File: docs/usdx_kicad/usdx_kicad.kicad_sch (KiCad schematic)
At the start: 0 parts

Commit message: Add KiCad PCB build files and ignore local artifacts
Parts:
- added C1, C29, C4: 1000u, Capacitor_THT:CP_Radial_D10.0mm_P5.00mm, symbol Device:C_Polarized
- added C10, C2, C3: 1n, Capacitor_THT:C_Disc_D5.0mm_W2.5mm_P5.00mm, symbol Device:C
- added C11, C12: 100p, Capacitor_THT:C_Disc_D5.0mm_W2.5mm_P5.00mm, symbol Device:C
- added C13, C18, C19, C21, C23, C26, C27: 100n, Capacitor_THT:C_Disc_D5.0mm_W2.5mm_P5.00mm, symbol Device:C
- added C14: 1u, Capacitor_THT:C_Disc_D5.0mm_W2.5mm_P5.00mm, symbol Device:C
- added C15, C16, C17, C20, C22, C24, C25, C28: 10u, Capacitor_THT:C_Disc_D5.0mm_W2.5mm_P5.00mm, symbol Device:C
- added C5, C6, C7, C8: 1n, Capacitor_THT:C_Rect_L11.5mm_W5.0mm_P10.00mm_MKT, symbol Device:C
- added C9: 470n, Capacitor_THT:C_Disc_D5.0mm_W2.5mm_P5.00mm, symbol Device:C
- added FST1: (no value), myFootprintLibrary:FST3253_board, symbol mySymbolLibrary:FST3253_board
- added J1: RX input, Connector_Coaxial:SMA_Molex_73251-1153_EdgeMount_Horizontal, symbol Connector:Conn_Coaxial
- added J10: Speaker, Connector_PinHeader_2.54mm:PinHeader_1x02_P2.54mm_Vertical, symbol Connector:Conn_01x02_Pin
- added J11: Power Connector, Connector_JST:JST_XH_B2B-XH-A_1x02_P2.50mm_Vertical, symbol Connector:Conn_01x02_Pin
- added J12: +12V, Connector_JST:JST_XH_B2B-XH-A_1x02_P2.50mm_Vertical, symbol Connector:Conn_01x02_Pin
- added J13: MCP23017, Connector_PinHeader_2.54mm:PinHeader_1x04_P2.54mm_Vertical, symbol Connector:Conn_01x04_Pin
- added J2: CLK2 output, Connector_Coaxial:SMA_Molex_73251-1153_EdgeMount_Horizontal, symbol Connector:Conn_Coaxial
- added J3: SSD1309, Connector_PinHeader_2.54mm:PinHeader_1x04_P2.54mm_Vertical, symbol Connector:Conn_01x04_Pin
- added J4: PWR SWR meter, Connector_PinHeader_2.54mm:PinHeader_1x03_P2.54mm_Vertical, symbol Connector:Conn_01x03_Pin
- added J5: W5500, Connector_PinHeader_2.54mm:PinHeader_1x08_P2.54mm_Vertical, symbol Connector:Conn_01x08_Pin
- added J6: ROT_MENU, Connector_PinHeader_2.54mm:PinHeader_1x05_P2.54mm_Vertical, symbol Connector:Conn_01x05_Pin
- added J7: ROT_FREQ, Connector_PinHeader_2.54mm:PinHeader_1x05_P2.54mm_Vertical, symbol Connector:Conn_01x05_Pin
- added J8: Button Right, Connector_PinHeader_2.54mm:PinHeader_1x02_P2.54mm_Vertical, symbol Connector:Conn_01x02_Pin
- added J9: Button Left, Connector_PinHeader_2.54mm:PinHeader_1x02_P2.54mm_Vertical, symbol Connector:Conn_01x02_Pin
- added L1, L2, L3, L4, L5, L6: 1mH, myFootprintLibrary:choke, symbol Device:L_Ferrite_Small
- added LM2596_board1, LM2596_board2: (no value), myFootprintLibrary:LM2596_board, symbol mySymbolLibrary:LM2596_board
- added MAX98357_board1: (no value), myFootprintLibrary:MAX98357_board, symbol mySymbolLibrary:MAX98357_board
- added PCM1: (no value), myFootprintLibrary:PCM1808_board, symbol mySymbolLibrary:PCM1808_board
- added R1, R2: 82K, Resistor_THT:R_Axial_DIN0207_L6.3mm_D2.5mm_P7.62mm_Horizontal, symbol Device:R_US
- added R10, R11, R3, R4, R5, R6: 100, Resistor_THT:R_Axial_DIN0207_L6.3mm_D2.5mm_P7.62mm_Horizontal, symbol Device:R_US
- added R12, R9: 1K, Resistor_THT:R_Axial_DIN0207_L6.3mm_D2.5mm_P7.62mm_Horizontal, symbol Device:R_US
- added R7, R8: 10K, Resistor_THT:R_Axial_DIN0207_L6.3mm_D2.5mm_P7.62mm_Horizontal, symbol Device:R_US
- added SI5351_board1: SI5351_board, myFootprintLibrary:SI5351_board, symbol mySymbolLibrary:SI5351_board
- added T1: Transformer_1P_1S, myFootprintLibrary:transformer, symbol Device:Transformer_1P_1S
- added U1: ESP32-S3-DevKitC, Espressif:ESP32-S3-DevKitC, symbol Espressif:ESP32-S3-DevKitC
- added U2: LM4562, Package_DIP:DIP-8_W7.62mm, symbol Amplifier_Operational:LM4562
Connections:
- new net: C2.2, R2.2, R4.1, U2.2 (-)
- new net: C7.1, FST1.11 (2B2), R4.2
- new net: R6.1, U2.5 (+)
- new net: C6.1, FST1.10 (2B1), R6.2
- new net: C8.1, FST1.12 (2B3), R5.2
- new net: C5.1, FST1.13 (2B4), R3.2
- new net: FST1.14 (S0), SI5351_board1.6 (CLK1)
- new net: C21.1, C22.1, FST1.16 (VCC), L3.1
- new net: FST1.2 (S1), SI5351_board1.7 (CLK0)
- new net: FST1.9 (2A), T1.3 (SA)
- new net: C10.1, C16.1, C9.1, R7.1, R8.2, T1.4 (SB)
- new net: J10.1 (Pin_1), MAX98357_board1.8 (O+)
- new net: J10.2 (Pin_2), MAX98357_board1.9 (O-)
- new net: C25.1, C26.1, C4.1, J12.1 (Pin_1), L5.2, LM2596_board2.3 (IN+)
- new net: C2.1, PCM1.15 (RIN), R2.1, U2.1
- new net: L6.1, LM2596_board2.2 (OUT+)
- new net: C19.1, C20.1, L2.1, U2.8 (V+)
- new net: C3.1, PCM1.13 (LIN), R1.1, U2.7
- new net: C3.2, R1.2, R3.1, U2.6 (-)
- new net: C1.1, J11.1 (Pin_1), LM2596_board1.3 (IN+)
- new net: C17.1, C18.1, L1.1, PCM1.6 (VCC+5)
- new net: R10.1, U1.38 (GPIO41/MTDI)
- new net: C23.1, C24.1, L4.1, SI5351_board1.1 (VCC)
- new net: R11.1, U1.39 (GPIO42/MTMS)
- new net: J2.1 (In), SI5351_board1.5 (CLK2)
- new net: J1.1 (In), T1.1 (AA)
- new net: J1.2 (Ext), T1.2 (AB)
- new net: L5.1, LM2596_board1.2 (OUT+)
- new net: J4.1 (Pin_1), U1.5 (GPIO5/ADC1_CH4)
- new net: J4.2 (Pin_2), U1.4 (GPIO4/ADC1_CH3)
- new net: R5.1, U2.3 (+)
- new net: MAX98357_board1.5 (DIN), U1.10 (GPIO17/ADC2_CH6)
- new net: MAX98357_board1.6 (BCLK), U1.9 (GPIO16/ADC2_CH5/32K_N)
- new net: MAX98357_board1.7 (LRC), U1.8 (GPIO15/ADC2_CH4/32K_P)
- new net: J5.3 (Pin_3), U1.11 (GPIO18/ADC2_CH7)
- new net: J5.4 (Pin_4), U1.12 (GPIO8/ADC1_CH7)
- new net: J5.7 (Pin_7), U1.40 (GPIO2/ADC1_CH1)
- new net: J5.8 (Pin_8), U1.41 (GPIO1/ADC1_CH0)
- new net: J5.6 (Pin_6), U1.6 (GPIO6/ADC1_CH5)
- new net: J5.5 (Pin_5), U1.7 (GPIO7/ADC1_CH6)
- new net +3.3V: C13.1, C14.1, C15.1, J13.4 (Pin_4), J3.4 (Pin_4), J5.1 (Pin_1), J6.2 (Pin_2), J7.2 (Pin_2), PCM1.5 (VDD+3.3), PCM1.7 (VDD+3.3), R12.2, R9.2, U1.1 (3V3), U1.2 (3V3)
- new net +5V: C27.1, C28.1, C29.1, L1.2, L2.2, L3.2, L4.2, L6.2, MAX98357_board1.1 (VCC), R7.2, U1.21 (5V)
- new net BTN_L: J9.1 (Pin_1), U1.20 (GPIO14/ADC2_CH3)
- new net BTN_R: J8.1 (Pin_1), U1.19 (GPIO13/ADC2_CH2)
- new net GND: C1.2, C10.2, C11.2, C12.2, C13.2, C14.2, C15.2, C16.2, C17.2, C18.2, C19.2, C20.2, C21.2, C22.2, C23.2, C24.2, C25.2, C26.2, C27.2, C28.2, C29.2, C4.2, C5.2, C6.2, C7.2, C8.2, C9.2, FST1.1 (OE1), FST1.15 (OE2), FST1.8 (GND), J11.2 (Pin_2), J12.2 (Pin_2), J13.3 (Pin_3), J2.2 (Ext), J3.3 (Pin_3), J4.3 (Pin_3), J5.2 (Pin_2), J6.1 (Pin_1), J7.1 (Pin_1), J8.2 (Pin_2), J9.2 (Pin_2), LM2596_board1.1 (OUT-), LM2596_board1.4 (IN-), LM2596_board2.1 (OUT-), LM2596_board2.4 (IN-), MAX98357_board1.2 (GND), PCM1.14 (GND), PCM1.4 (GND), PCM1.8 (GND), R8.1, SI5351_board1.2 (GND), U1.22 (GND), U1.23 (GND), U1.24 (GND), U1.44 (GND), U2.4 (V-)
- new net I2C_SCL: C11.1, J13.2 (Pin_2), J3.2 (Pin_2), R11.2, R12.1, SI5351_board1.4 (SCL)
- new net I2C_SDA: C12.1, J13.1 (Pin_1), J3.1 (Pin_1), R10.2, R9.1, SI5351_board1.3 (SDA)
- new net I2S_BCK_PCM1808: PCM1.12 (BCK), U1.18 (GPIO12/ADC2_CH1)
- new net I2S_LRC_PCM1808: PCM1.10 (LRC), U1.16 (GPIO10/ADC1_CH9)
- new net I2S_OUT_PCM1808: PCM1.11 (OUT), U1.17 (GPIO11/ADC2_CH0)
- new net I2S_SCK_PCM1808: PCM1.9 (SCK), U1.15 (GPIO9/ADC1_CH8)
- new net ROT_FREQ_CLK: J7.5 (Pin_5), U1.27 (GPIO21)
- new net ROT_FREQ_DT: J7.4 (Pin_4), U1.28 (GPIO47)
- new net ROT_FREQ_SW: J7.3 (Pin_3), U1.30 (GPIO45)
- new net ROT_MENU_CLK: J6.5 (Pin_5), U1.35 (GPIO38)
- new net ROT_MENU_DT: J6.4 (Pin_4), U1.36 (GPIO39/MTCK)
- new net ROT_MENU_SW: J6.3 (Pin_3), U1.37 (GPIO40/MTDO)
- no-connect marks 0 -> 22
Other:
- company: (none) -> Guido Giorgetti - IW5ALZ

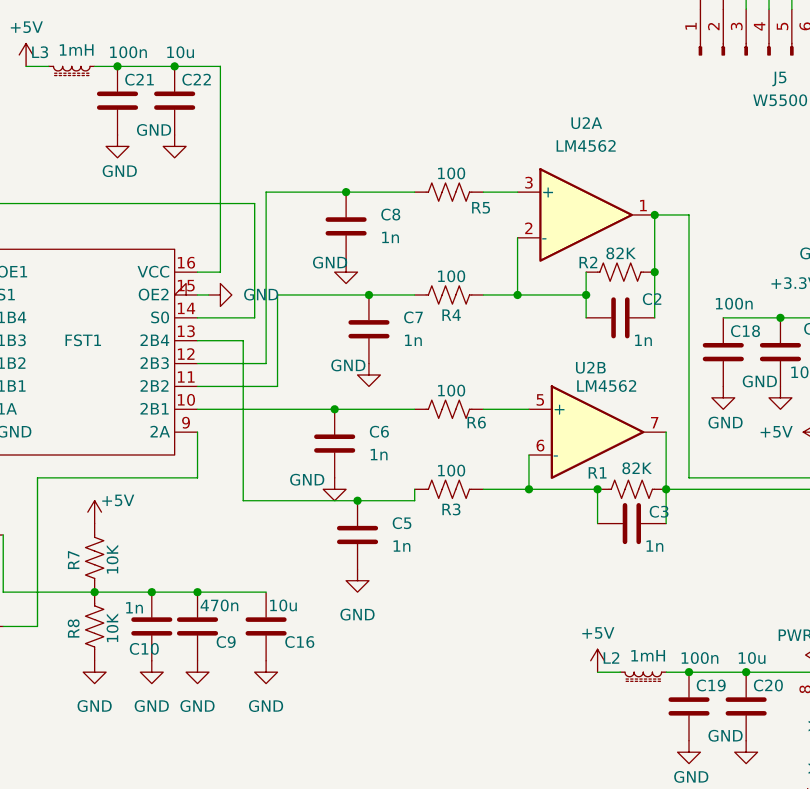
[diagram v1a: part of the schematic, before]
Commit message: LM4562 DC decoupling
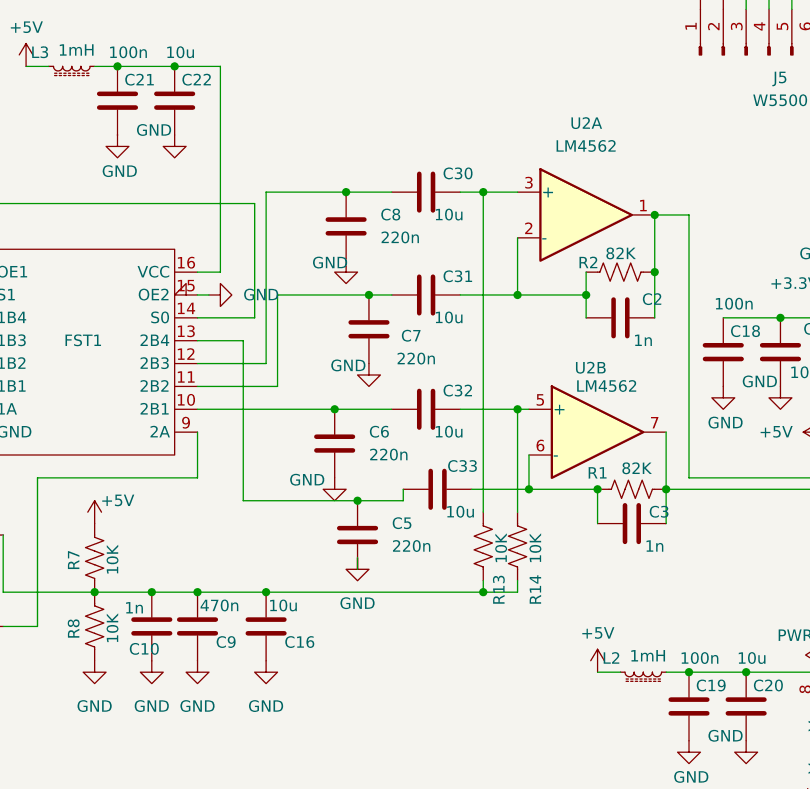
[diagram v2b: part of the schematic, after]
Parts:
- removed R3, R4, R5, R6: 100, Resistor_THT:R_Axial_DIN0207_L6.3mm_D2.5mm_P7.62mm_Horizontal, symbol Device:R_US
- added C30, C31, C32, C33: 10u, Capacitor_THT:C_Disc_D5.0mm_W2.5mm_P5.00mm, symbol Device:C
- added R13, R14: 10K, Resistor_THT:R_Axial_DIN0207_L6.3mm_D2.5mm_P7.62mm_Horizontal, symbol Device:R_US
- C5, C6, C7, C8: value 1n -> 220n
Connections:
- net at C2.2, R2.2, U2.2 (-): now also C31.1
- net at C7.1, FST1.11 (2B2): now also C31.2
- net at U2.5 (+): now also C32.1, R14.2
- net at C6.1, FST1.10 (2B1): now also C32.2
- net at C8.1, FST1.12 (2B3): now also C30.2
- net at C5.1, FST1.13 (2B4): now also C33.2
- net at C10.1, C16.1, C9.1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: now also R13.1, R14.1
- net at C3.2, R1.2, U2.6 (-): now also C33.1
- net at U2.3 (+): now also C30.1, R13.2

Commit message: PCB version 1.1
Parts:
- removed J1: RX input, Connector_Coaxial:SMA_Molex_73251-1153_EdgeMount_Horizontal, symbol Connector:Conn_Coaxial
- removed J2: CLK2 output, Connector_Coaxial:SMA_Molex_73251-1153_EdgeMount_Horizontal, symbol Connector:Conn_Coaxial
- added U3: RX Input, myFootprintLibrary:SMA connector, symbol mySymbolLibrary:SMA_Connector
- added U4: TX Out, myFootprintLibrary:SMA connector, symbol mySymbolLibrary:SMA_Connector
- U1: footprint Espressif:ESP32-S3-DevKitC -> myFootprintLibrary:ESP32-S3-DevKitC-Mine
- renumbered FST1 to FST3253
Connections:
- net GND: now also U4.1 (GND)
- net at SI5351_board1.5 (CLK2): now also U4.2 (RF)
- net at T1.1 (AA): now also U3.2 (RF)
- net at T1.2 (AB): now also U3.1 (GND)
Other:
- title: (none) -> FT8 ESP32

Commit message: capacitors voltage
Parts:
- C1: value 1000u -> 1000u 35V
- C29, C4: value 1000u -> 1000u 16V
- J11: value Power Connector -> Power Connector 19V
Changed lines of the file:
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@@
 		(dnp no)
 		(property "Reference" "C25"
-			(at 257.048 115.57 0)
+			(at 256.54 113.792 0)
 			(show_name no)
 			(do_not_autoplace no)
@@
 		)
 		(property "Value" "10u"
-			(at 259.334 124.46 0)
+			(at 256.794 116.586 0)
 			(show_name no)
 			(do_not_autoplace no)
@@
 			)
 		)
-		(property "Value" "Power Connector"
+		(property "Value" "Power Connector 19V"
 			(at 221.615 74.93 0)
 			(show_name no)
@@
 		(dnp no)
 		(property "Reference" "C26"
-			(at 252.222 119.634 0)
+			(at 250.698 113.792 0)
 			(show_name no)
 			(do_not_autoplace no)
@@
 			)
 		)
-		(property "Value" "1000u"
+		(property "Value" "1000u 35V"
 			(at 257.81 81.6609 0)
 			(show_name no)
@@
 			)
 		)
-		(property "Value" "1000u"
+		(property "Value" "1000u 16V"
 			(at 270.51 152.7809 0)
 			(show_name no)
@@
 		(dnp no)
 		(property "Reference" "C4"
-			(at 269.24 119.7609 0)
+			(at 263.906 113.792 0)
 			(show_name no)
 			(do_not_autoplace no)
@@
 			)
 		)
-		(property "Value" "1000u"
-			(at 266.446 124.714 0)
+		(property "Value" "1000u 16V"
+			(at 263.652 116.586 0)
 			(show_name no)
 			(do_not_autoplace no)
